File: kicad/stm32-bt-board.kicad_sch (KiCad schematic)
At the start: 0 parts

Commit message: feat(schematic): add hierarchical sheets, add STM32WB55CEUx power circuitry, and oscillator circuitry, and design notes
add STM32WB55CEUx symbol and rename package variant suffix from X to 6 to explicitly target the "Industrial temperature range, -40 to 85 °C (105 °C junction)"

add recommended MCU power decoupling network with a few tweaks following phil's video:
- 100nF capacitor per VDD-related supply pin placed locally
- 4.7uF bulk capacitors for VDD and VDDSMPS near the package

add buck converter topology for the integrated SMPS, suitable for the 4MHz switching frequency, for best power performance

add HSE and LSE crystal oscillator circuits (incomplete)

add schematic notes and reference links from STM32WB SMPS and oscillator layout/design guideline application notes
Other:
- added sheet Microcontroller (mcu.kicad_sch)
- title: (none) -> STM32 BT Tutorial Board
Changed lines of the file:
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@@
 	(generator_version "10.0")
 	(paper "A4")
+	(title_block
+		(title "STM32 BT Tutorial Board")
+		(date "2026-05-15")
+		(rev "1.0")
+		(comment 4 "GitHub: https://github.com/odaij/stm32-bt-board")
+	)
+	(sheet
+		(at 82.55 72.39)
+		(size 36.83 58.42)
+		(exclude_from_sim no)
+		(in_bom yes)
+		(on_board yes)
+		(dnp no)
+		(fields_autoplaced yes)
+		(stroke
+			(width 0.1524)
+			(type solid)
+		)
+		(fill
+			(color 194 0 0 1)
+		)
+		(property "Sheetname" "Microcontroller"
+			(at 82.55 71.1704 0)
+			(show_name no)
+			(do_not_autoplace no)
+			(effects
+				(font
+					(size 2.286 2.286)
+					(thickness 0.4572)
+					(bold yes)
+				)
+				(justify left bottom)
+			)
+		)
+		(property "Sheetfile" "mcu.kicad_sch"
+			(at 82.55 131.3946 0)
+			(show_name no)
+			(do_not_autoplace no)
+			(effects
+				(font
+					(size 1.27 1.27)
+				)
+				(justify left top)
+			)
+		)
+		(instances
+			(project "stm32-bt-board"
+				(path "/9ab97115-0b3b-4897-8d44-f79e27c270d1"
+					(page "2")
+				)
+			)
+		)
+	)
 	(sheet_instances
 		(path "/"

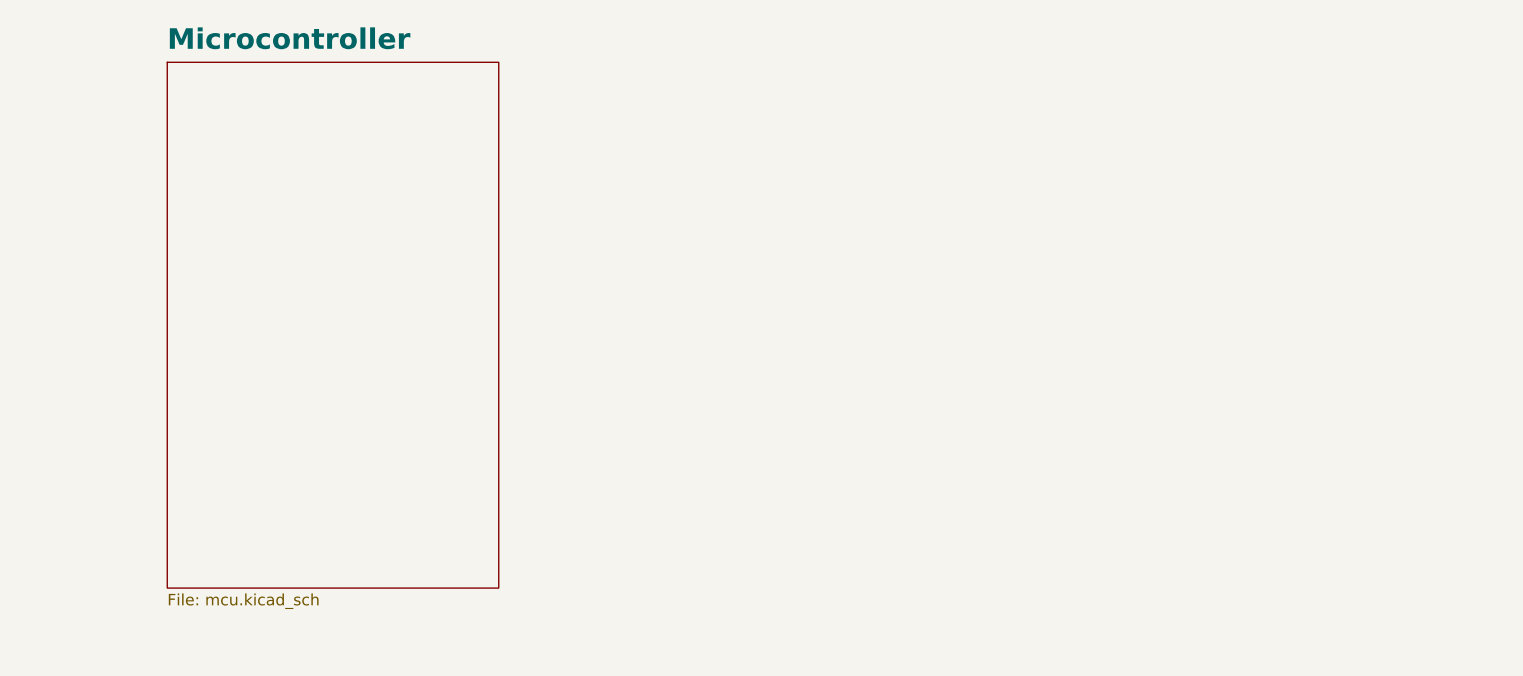
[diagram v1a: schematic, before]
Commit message: feat (schematic): add basmala to root, create new hierarchical sheet for usb inside root, and more /stm32-bt-board/ add basmala to root schematic - add a new usb hierarchical sheet to root
/stm32-bt-board/Microcontroller/
- add resistance value for BOOT0 LPF

/stm32-bt-board/USB/
- add usb type c receptacle
- add the usblc6-2sc6 protection ic to D- and D+
- add 5k1 pull down resistors for CC1 and CC2
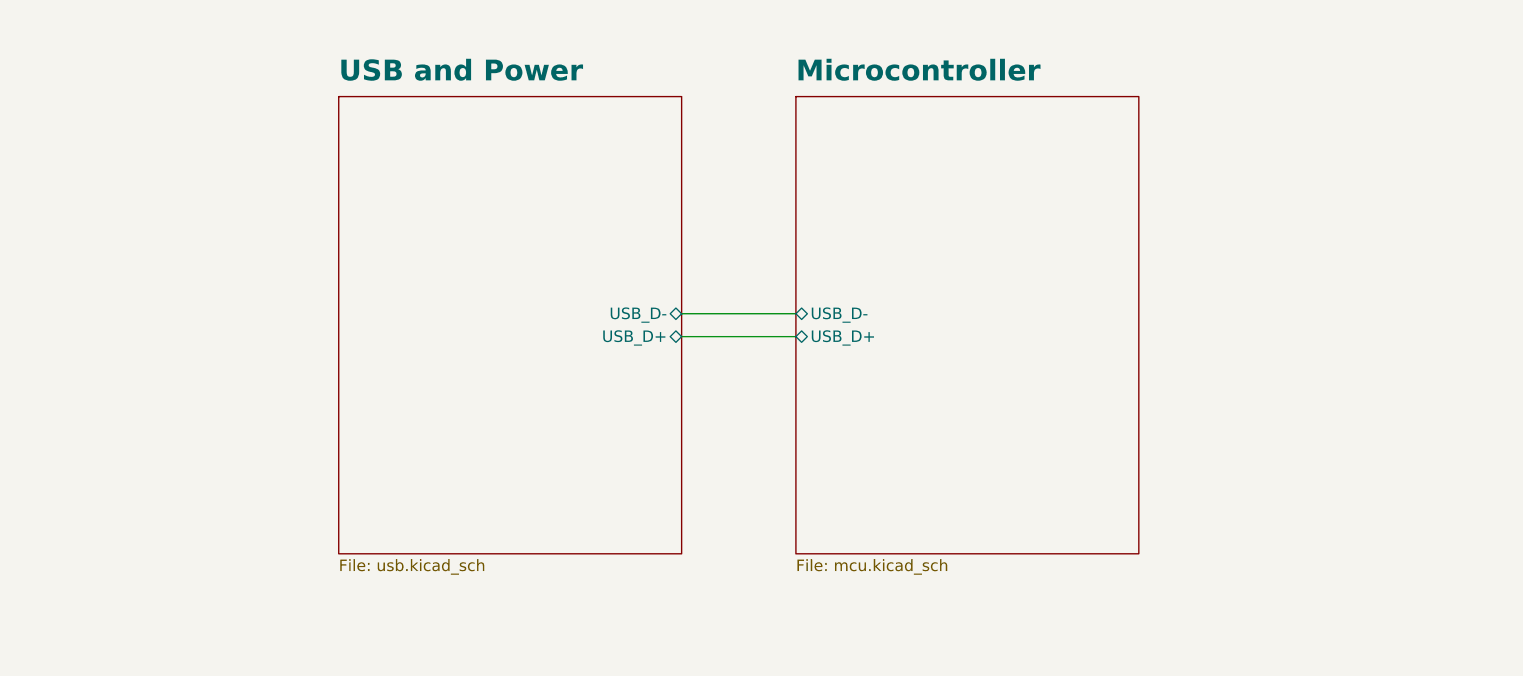
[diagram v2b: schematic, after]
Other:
- added sheet USB and Power (usb.kicad_sch)
- sheet Microcontroller ports: added USB_D+, USB_D-; removed none

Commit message: A LOT OF STUFF
I almost finished the schematic part of the tutorial
what remains is part choosing and filling the relevant fields for every component
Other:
- sheet USB and Power renamed Power
- added sheet USB (usb.kicad_sch)
- sheet Power: file usb.kicad_sch -> power.kicad_sch
- sheet Power ports: added none; removed USB_D+, USB_D-
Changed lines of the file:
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@@
 	(title_block
 		(title "STM32 BT Tutorial Board")
-		(date "2026-05-15")
+		(date "2026-05-27")
 		(rev "1.0")
 		(comment 4 "GitHub: https://github.com/odaij/stm32-bt-board")
@@
 	(wire
 		(pts
-			(xy 139.7 102.87) (xy 152.4 102.87)
+			(xy 167.64 90.17) (xy 193.04 90.17)
 		)
 		(stroke
@@
 	(wire
 		(pts
-			(xy 139.7 100.33) (xy 152.4 100.33)
+			(xy 167.64 87.63) (xy 193.04 87.63)
 		)
 		(stroke
@@
 	)
 	(sheet
-		(at 101.6 76.2)
+		(at 66.04 85.09)
 		(size 38.1 50.8)
 		(exclude_from_sim no)
@@
 			(color 111 117 255 1)
 		)
-		(property "Sheetname" "USB and Power"
-			(at 101.6 74.676 0)
+		(property "Sheetname" "Power"
+			(at 66.04 83.566 0)
 			(show_name no)
 			(do_not_autoplace no)
@@
 			)
 		)
-		(property "Sheetfile" "usb.kicad_sch"
-			(at 101.6 127.5846 0)
+		(property "Sheetfile" "power.kicad_sch"
+			(at 66.04 136.4746 0)
 			(show_name no)
 			(do_not_autoplace no)
@@
 			)
 		)
-		(pin "USB_D+" bidirectional
-			(at 139.7 102.87 0)
-			(effects
-				(font
-					(size 1.27 1.27)
-					(color 0 0 0 1)
-				)
-				(justify right)
-			)
-		)
-		(pin "USB_D-" bidirectional
-			(at 139.7 100.33 0)
-			(effects
-				(font
-					(size 1.27 1.27)
-					(color 0 0 0 1)
-				)
-				(justify right)
-			)
-		)
 		(instances
 			(project "stm32-bt-board"
@@
 	)
 	(sheet
-		(at 152.4 76.2)
+		(at 193.04 85.09)
 		(size 38.1 50.8)
 		(exclude_from_sim no)
@@
 		)
 		(property "Sheetname" "Microcontroller"
-			(at 152.4 74.676 0)
+			(at 193.04 83.566 0)
 			(show_name no)
 			(do_not_autoplace no)
@@
 		)
 		(property "Sheetfile" "mcu.kicad_sch"
-			(at 152.4 127.5846 0)
+			(at 193.04 136.4746 0)
 			(show_name no)
 			(do_not_autoplace no)
@@
 		)
 		(pin "USB_D+" bidirectional
-			(at 152.4 102.87 180)
+			(at 193.04 90.17 180)
 			(effects
 				(font
@@
 		)
 		(pin "USB_D-" bidirectional
-			(at 152.4 100.33 180)
+			(at 193.04 87.63 180)
 			(effects
 				(font
@@
 				)
 			)
+		)
+	)
+	(sheet
+		(at 129.54 85.09)
+		(size 38.1 50.8)
+		(exclude_from_sim no)
+		(in_bom yes)
+		(on_board yes)
+		(dnp no)
+		(fields_autoplaced yes)
+		(stroke
+			(width 0.1524)
+			(type solid)
+		)
+		(fill
+			(color 141 255 49 1)
+		)
+		(property "Sheetname" "USB"
+			(at 129.54 83.8634 0)
+			(show_name no)
+			(do_not_autoplace no)
+			(effects
+				(font
+					(size 2.3 2.3)
+					(thickness 0.46)
+					(bold yes)
+				)
+				(justify left bottom)
+			)
+		)
+		(property "Sheetfile" "usb.kicad_sch"
+			(at 129.54 136.4746 0)
+			(show_name no)
+			(do_not_autoplace no)
+			(effects
+				(font
+					(size 1.27 1.27)
+				)
+				(justify left top)
+			)
+		)
+		(pin "USB_D+" bidirectional
+			(at 167.64 90.17 0)
+			(effects
+				(font
+					(size 1.27 1.27)
+				)
+				(justify right)
+			)
+		)
+		(pin "USB_D-" bidirectional
+			(at 167.64 87.63 0)
+			(effects
+				(font
+					(size 1.27 1.27)
+				)
+				(justify right)
+			)
+		)
+		(instances
+			(project "stm32-bt-board"
+				(path "/9ab97115-0b3b-4897-8d44-f79e27c270d1"
+					(page "4")
+				)
+			)

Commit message: refactor(schematic): polish the schematic as much as possible - add new Basmala - fix netlist names almost EVERYWHERE, this is to help with net classes, and to help with building a good habit of naming nets properly - add a 100n capacitor to the SWD connector power pin - update many many other things EVERYWHERE
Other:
- sheet Power renamed LDO
- removed sheet USB
- added sheet Connectors (connectors.kicad_sch)
- sheet LDO: file power.kicad_sch -> ldo.kicad_sch
- sheet Microcontroller ports: added SWCLK, SWDIO, SWO, UART_RX, UART_TX; removed none
- note added: "+3V3"
- note added: "+5V"
- note added: "TODO: - assign footprints - finish page setup (A4, title, github repo link) - table of contents? block diagram? feeling fancy - 3V3_UART, and 3V3_SWD along with 0 ohm resistors for better netnames?"
